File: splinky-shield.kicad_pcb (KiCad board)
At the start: 2 copper layers, 73.5 x 50.8 mm, 61 parts, among them J1 USB_C_Receptacle_USB2.0, J10 Ribbon, J11 Serial, J12 Conn_01x04_Female, J13 Conn_01x02_Female, J2 Conn_01x04_Female, J3 Conn_01x04_Female, J4 Conn_01x04_Female, J5 Conn_01x02, J6 Serial, J7 trackball, J8 Ribbon, J9 RGB, U1 RP2040, U2 GD25Q80CEIGR, U3 XC6210B332MR-G, U4 USBLC6-2P6, Y1 Crystal_GND24

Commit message: drc
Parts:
- moved FB1 9.92 mm to (197.2, 90.8)
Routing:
- net Net-(FB1-Pad2): track 25.7 -> 2.52 mm
- net /Gnd_daughter: track 22.8 -> 17.3 mm, vias 6 -> 5
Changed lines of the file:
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@@
   )
   (footprint "Inductor_SMD:L_0603_1608Metric" (layer "F.Cu")
-    (at 187.53 92.88 90)
+    (at 197.23 90.81 90)
     (descr "Inductor SMD 0603 (1608 Metric), square (rectangular) end terminal, IPC_7351 nominal, (Body size source: http://www.tortai-tech.com/upload/download/2011102023233369053.pdf), generated with kicad-footprint-generator")
     (tags "inductor")
@@
   (segment (start 155.55 90.5) (end 155.55 85.79) (width 0.16) (layer "F.Cu") (net 10))
   (via (at 155.55 90.5) (size 0.6) (drill 0.3) (layers "F.Cu" "B.Cu") (net 10))
-  (segment (start 186.585 88.496) (end 186.585 91.1475) (width 0.4) (layer "F.Cu") (net 11))
-  (segment (start 186.585 91.1475) (end 187.53 92.0925) (width 0.4) (layer "F.Cu") (net 11))
-  (segment (start 196.061 90.17) (end 197.735 88.496) (width 0.4) (layer "B.Cu") (net 11))
-  (segment (start 188.259 90.17) (end 196.061 90.17) (width 0.4) (layer "B.Cu") (net 11))
-  (segment (start 186.585 88.496) (end 188.259 90.17) (width 0.4) (layer "B.Cu") (net 11))
-  (segment (start 186.585 83.896) (end 186.585 88.496) (width 0.4) (layer "B.Cu") (net 11))
-  (segment (start 197.735 88.496) (end 197.735 83.896) (width 0.4) (layer "B.Cu") (net 11))
+  (segment (start 197.78 89.4725) (end 197.23 90.0225) (width 0.25) (layer "F.Cu") (net 11))
+  (segment (start 197.78 87.73) (end 197.78 89.4725) (width 0.25) (layer "F.Cu") (net 11))
   (segment (start 193.828438 91.171562) (end 193.41 90.753124) (width 0.2) (layer "F.Cu") (net 13))
   (segment (start 194.13 92.03) (end 193.828438 91.728438) (width 0.2) (layer "F.Cu") (net 13))
@@
   (via (at 194.57 91.03) (size 0.6) (drill 0.3) (layers "F.Cu" "B.Cu") (net 65))
   (via (at 189.76 91.03) (size 0.6) (drill 0.3) (layers "F.Cu" "B.Cu") (net 65))
-  (segment (start 198.54 87.53) (end 199.78 86.29) (width 0.25) (layer "B.Cu") (net 65))
   (segment (start 190.21 91.48) (end 189.76 91.03) (width 0.25) (layer "B.Cu") (net 65))
   (segment (start 192.17 91.48) (end 190.21 91.48) (width 0.25) (layer "B.Cu") (net 65))
+  (segment (start 198.47 88.535558) (end 198.75 88.255558) (width 0.25) (layer "B.Cu") (net 65))
+  (segment (start 197.12 91.14) (end 198.47 89.79) (width 0.25) (layer "B.Cu") (net 65))
   (segment (start 192.17 91.48) (end 194.12 91.48) (width 0.25) (layer "B.Cu") (net 65))
-  (segment (start 197.12 91.14) (end 198.54 89.72) (width 0.25) (layer "B.Cu") (net 65))
-  (segment (start 198.54 89.72) (end 198.54 87.53) (width 0.25) (layer "B.Cu") (net 65))
-  (segment (start 187.06 91.03) (end 185.78 89.75) (width 0.25) (layer "B.Cu") (net 65))
-  (segment (start 194.67 91.14) (end 197.12 91.14) (width 0.25) (layer "B.Cu") (net 65))
+  (segment (start 198.75 87.32) (end 199.78 86.29) (width 0.25) (layer "B.Cu") (net 65))
+  (segment (start 194.57 91.03) (end 194.57 91.04) (width 0.25) (layer "B.Cu") (net 65))
+  (segment (start 187.06 91.03) (end 185.669511 89.639511) (width 0.25) (layer "B.Cu") (net 65))
   (segment (start 194.12 91.48) (end 194.57 91.03) (width 0.25) (layer "B.Cu") (net 65))
+  (segment (start 198.75 88.255558) (end 198.75 87.32) (width 0.25) (layer "B.Cu") (net 65))
   (segment (start 194.57 91.04) (end 194.67 91.14) (width 0.25) (layer "B.Cu") (net 65))
-  (segment (start 185.78 89.75) (end 185.78 87.535) (width 0.25) (layer "B.Cu") (net 65))
-  (segment (start 185.78 87.535) (end 184.535 86.29) (width 0.25) (layer "B.Cu") (net 65))
+  (segment (start 185.669511 89.639511) (end 185.669511 87.424511) (width 0.25) (layer "B.Cu") (net 65))
+  (segment (start 194.67 91.14) (end 197.12 91.14) (width 0.25) (layer "B.Cu") (net 65))
+  (segment (start 198.47 89.79) (end 198.47 88.535558) (width 0.25) (layer "B.Cu") (net 65))
+  (segment (start 185.669511 87.424511) (end 184.535 86.29) (width 0.25) (layer "B.Cu") (net 65))
   (segment (start 189.76 91.03) (end 187.06 91.03) (width 0.25) (layer "B.Cu") (net 65))
-  (segment (start 194.57 91.03) (end 194.57 91.04) (width 0.25) (layer "B.Cu") (net 65))
   (segment (start 189.94 93.05) (end 189.7 93.05) (width 0.2) (layer "F.Cu") (net 66))
-  (segment (start 185.87 91.57) (end 185.87 91.834933) (width 0.2) (layer "F.Cu") (net 66))
-  (segment (start 184.535 88.83) (end 185.87 90.165) (width 0.2) (layer "F.Cu") (net 66))
   (segment (start 194.94 93.05) (end 195.14 92.85) (width 0.2) (layer "F.Cu") (net 66))
   (segment (start 195.36 88.93) (end 195.36 91.1945) (width 0.25) (layer "F.Cu") (net 66))
@@
   (segment (start 192.17 93.922991) (end 192.17 94.347013) (width 0.2) (layer "F.Cu") (net 66))
   (segment (start 188.96 89.901) (end 188.96 88.93) (width 0.2) (layer "F.Cu") (net 66))
+  (segment (start 197.23 91.5975) (end 197.23 91.76) (width 0.25) (layer "F.Cu") (net 66))
   (segment (start 195.36 91.1945) (end 195.89 91.7245) (width 0.25) (layer "F.Cu") (net 66))
   (segment (start 189.7 93.05) (end 189.39 92.74) (width 0.2) (layer "F.Cu") (net 66))
-  (segment (start 187.53 93.6675) (end 187.53 93.494933) (width 0.2) (layer "F.Cu") (net 66))
-  (segment (start 185.87 90.165) (end 185.87 91.57) (width 0.2) (layer "F.Cu") (net 66))
   (segment (start 192.027013 94.49) (end 191.42 94.49) (width 0.2) (layer "F.Cu") (net 66))
+  (segment (start 197.525457 92.055457) (end 196.730913 92.85) (width 0.2) (layer "F.Cu") (net 66))
   (segment (start 194.399916 93.05) (end 194.94 93.05) (width 0.2) (layer "F.Cu") (net 66))
   (segment (start 191.42 94.49) (end 190.52 94.49) (width 0.2) (layer "F.Cu") (net 66))
   (segment (start 190.52 94.49) (end 190.26 94.23) (width 0.2) (layer "F.Cu") (net 66))
-  (segment (start 185.87 91.834933) (end 186.932422 92.897355) (width 0.2) (layer "F.Cu") (net 66))
-  (segment (start 187.53 93.494933) (end 186.932422 92.897355) (width 0.2) (layer "F.Cu") (net 66))
   (segment (start 196.730913 92.85) (end 195.14 92.85) (width 0.2) (layer "F.Cu") (net 66))
-  (segment (start 199.78 89.800913) (end 196.730913 92.85) (width 0.2) (layer "F.Cu") (net 66))
+  (segment (start 199.78 89.800913) (end 197.525457 92.055457) (width 0.2) (layer "F.Cu") (net 66))
   (segment (start 188.91 89.951) (end 188.91 91.44) (width 0.2) (layer "F.Cu") (net 66))
   (segment (start 192.17 94.347013) (end 192.027013 94.49) (width 0.2) (layer "F.Cu") (net 66))
   (segment (start 188.91 91.44) (end 188.7 91.65) (width 0.2) (layer "F.Cu") (net 66))
   (segment (start 188.91 89.951) (end 188.96 89.901) (width 0.2) (layer "F.Cu") (net 66))
+  (segment (start 197.23 91.76) (end 197.525457 92.055457) (width 0.25) (layer "F.Cu") (net 66))
   (via (at 195.89 91.7245) (size 0.6) (drill 0.3) (layers "F.Cu" "B.Cu") (net 66))
-  (via (at 186.932422 92.897355) (size 0.6) (drill 0.3) (layers "F.Cu" "B.Cu") (net 66))
   (via (at 189.39 92.74) (size 0.6) (drill 0.3) (layers "F.Cu" "B.Cu") (net 66))
   (via (at 195.14 92.85) (size 0.6) (drill 0.3) (layers "F.Cu" "B.Cu") (net 66))

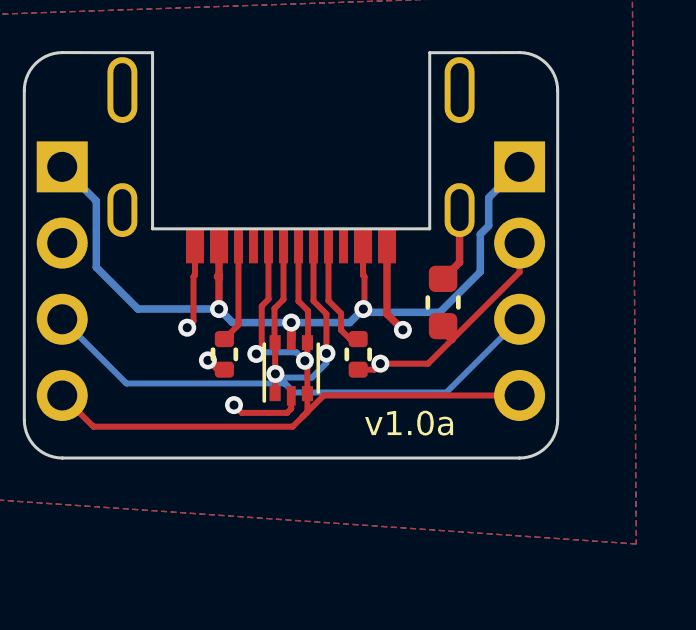
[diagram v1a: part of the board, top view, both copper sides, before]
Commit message: move daughterboard components to accomodate usb-c
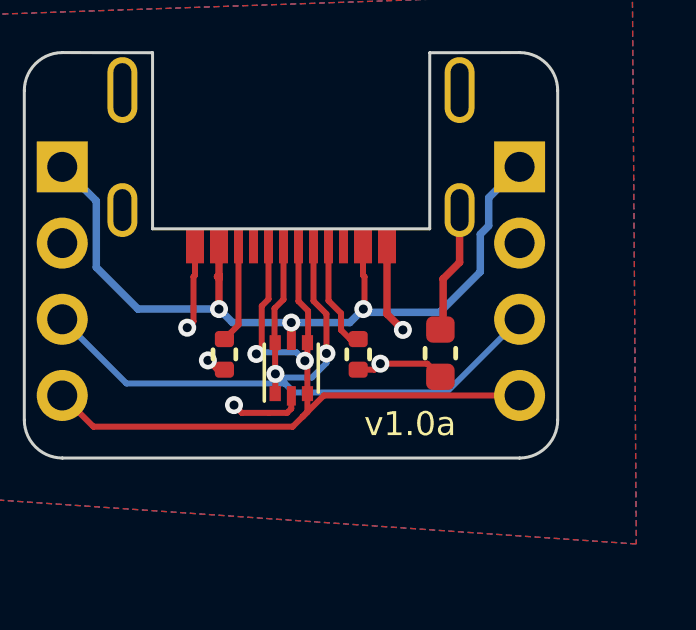
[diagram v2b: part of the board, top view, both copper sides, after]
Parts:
- moved FB1 1.69 mm to (197.1, 92.5)
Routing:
- net /Gnd_daughter: track 17.3 -> 12.0 mm
- net Net-(FB1-Pad2): track 2.52 -> 4.25 mm
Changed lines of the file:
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@@
   )
   (footprint "Inductor_SMD:L_0603_1608Metric" (layer "F.Cu")
-    (at 197.23 90.81 90)
+    (at 197.14 92.5 90)
     (descr "Inductor SMD 0603 (1608 Metric), square (rectangular) end terminal, IPC_7351 nominal, (Body size source: http://www.tortai-tech.com/upload/download/2011102023233369053.pdf), generated with kicad-footprint-generator")
     (tags "inductor")
@@
   (via (at 155.55 90.5) (size 0.6) (drill 0.3) (layers "F.Cu" "B.Cu") (net 10))
   (segment (start 197.78 89.4725) (end 197.23 90.0225) (width 0.25) (layer "F.Cu") (net 11))
+  (segment (start 197.23 90.0225) (end 197.23 91.6225) (width 0.25) (layer "F.Cu") (net 11))
+  (segment (start 197.23 91.6225) (end 197.14 91.7125) (width 0.25) (layer "F.Cu") (net 11))
   (segment (start 197.78 87.73) (end 197.78 89.4725) (width 0.25) (layer "F.Cu") (net 11))
   (segment (start 193.828438 91.171562) (end 193.41 90.753124) (width 0.2) (layer "F.Cu") (net 13))
@@
   (segment (start 194.94 93.05) (end 195.14 92.85) (width 0.2) (layer "F.Cu") (net 66))
   (segment (start 195.36 88.93) (end 195.36 91.1945) (width 0.25) (layer "F.Cu") (net 66))
-  (segment (start 199.78 88.83) (end 199.78 89.800913) (width 0.2) (layer "F.Cu") (net 66))
   (segment (start 192.17 93.922991) (end 192.17 94.347013) (width 0.2) (layer "F.Cu") (net 66))
   (segment (start 188.96 89.901) (end 188.96 88.93) (width 0.2) (layer "F.Cu") (net 66))
-  (segment (start 197.23 91.5975) (end 197.23 91.76) (width 0.25) (layer "F.Cu") (net 66))
+  (segment (start 195.14 92.85) (end 196.7025 92.85) (width 0.2) (layer "F.Cu") (net 66))
   (segment (start 195.36 91.1945) (end 195.89 91.7245) (width 0.25) (layer "F.Cu") (net 66))
   (segment (start 189.7 93.05) (end 189.39 92.74) (width 0.2) (layer "F.Cu") (net 66))
   (segment (start 192.027013 94.49) (end 191.42 94.49) (width 0.2) (layer "F.Cu") (net 66))
-  (segment (start 197.525457 92.055457) (end 196.730913 92.85) (width 0.2) (layer "F.Cu") (net 66))
+  (segment (start 196.7025 92.85) (end 197.14 93.2875) (width 0.2) (layer "F.Cu") (net 66))
   (segment (start 194.399916 93.05) (end 194.94 93.05) (width 0.2) (layer "F.Cu") (net 66))
   (segment (start 191.42 94.49) (end 190.52 94.49) (width 0.2) (layer "F.Cu") (net 66))
   (segment (start 190.52 94.49) (end 190.26 94.23) (width 0.2) (layer "F.Cu") (net 66))
-  (segment (start 196.730913 92.85) (end 195.14 92.85) (width 0.2) (layer "F.Cu") (net 66))
-  (segment (start 199.78 89.800913) (end 197.525457 92.055457) (width 0.2) (layer "F.Cu") (net 66))
   (segment (start 188.91 89.951) (end 188.91 91.44) (width 0.2) (layer "F.Cu") (net 66))
   (segment (start 192.17 94.347013) (end 192.027013 94.49) (width 0.2) (layer "F.Cu") (net 66))
   (segment (start 188.91 91.44) (end 188.7 91.65) (width 0.2) (layer "F.Cu") (net 66))
   (segment (start 188.91 89.951) (end 188.96 89.901) (width 0.2) (layer "F.Cu") (net 66))
-  (segment (start 197.23 91.76) (end 197.525457 92.055457) (width 0.25) (layer "F.Cu") (net 66))
   (via (at 195.89 91.7245) (size 0.6) (drill 0.3) (layers "F.Cu" "B.Cu") (net 66))
   (via (at 189.39 92.74) (size 0.6) (drill 0.3) (layers "F.Cu" "B.Cu") (net 66))
